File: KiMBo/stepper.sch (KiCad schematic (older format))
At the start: 17 parts

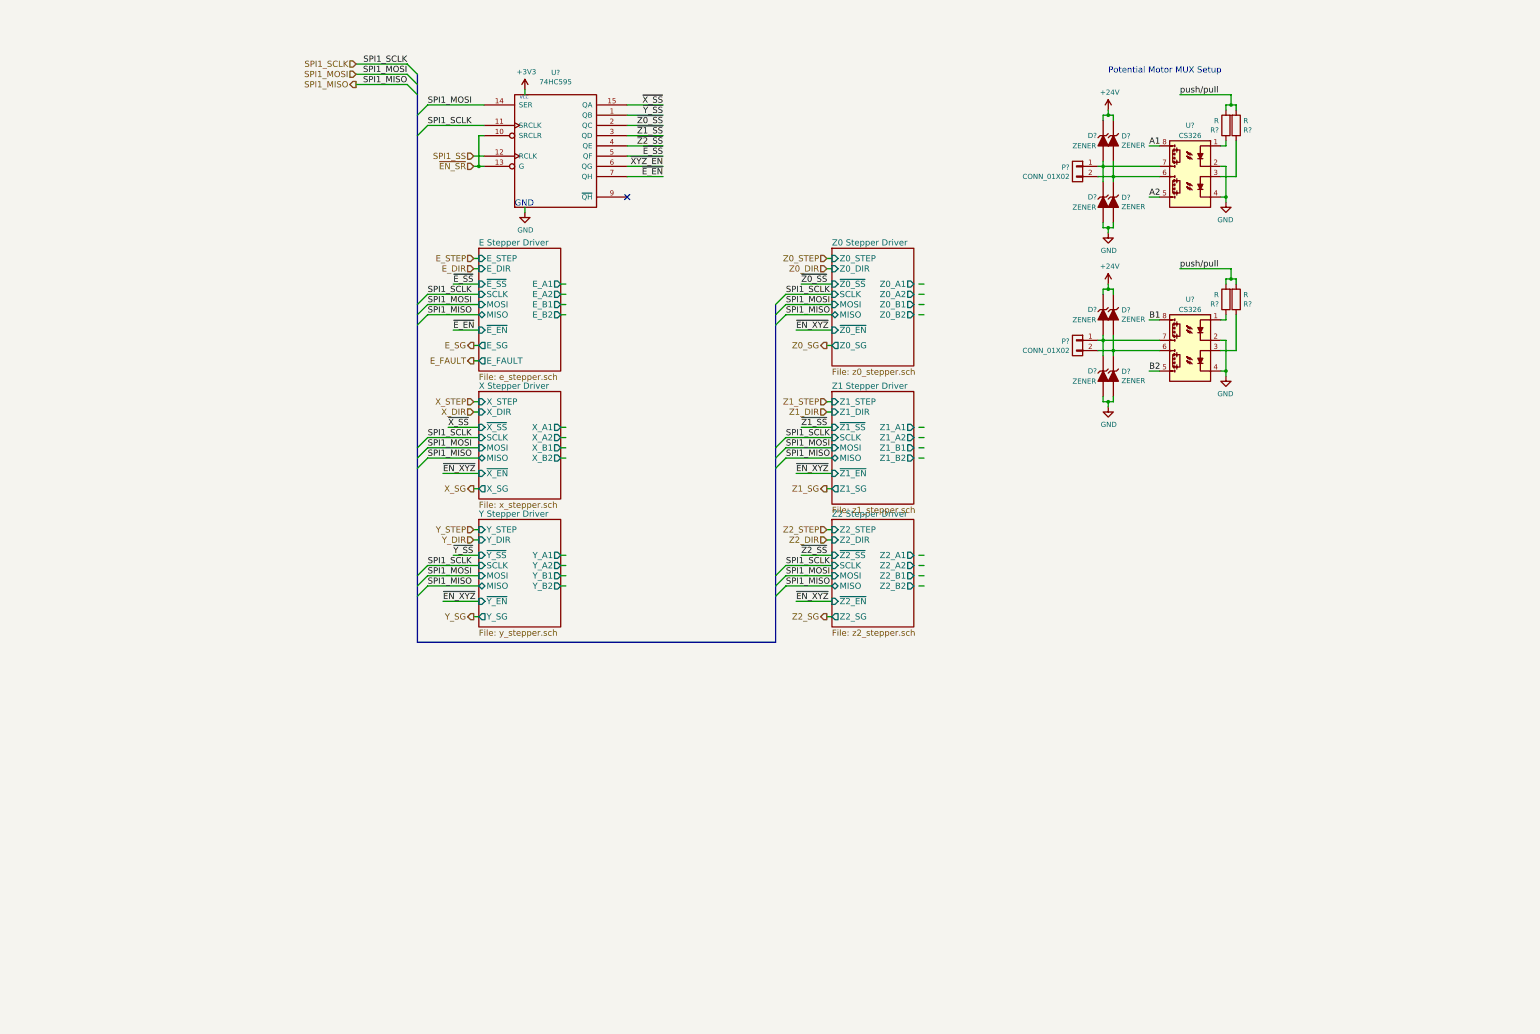
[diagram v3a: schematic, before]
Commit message: Update the fixed Vain voltage and begin placing connectors at the highest level (root) of the hierarchical sheet structure
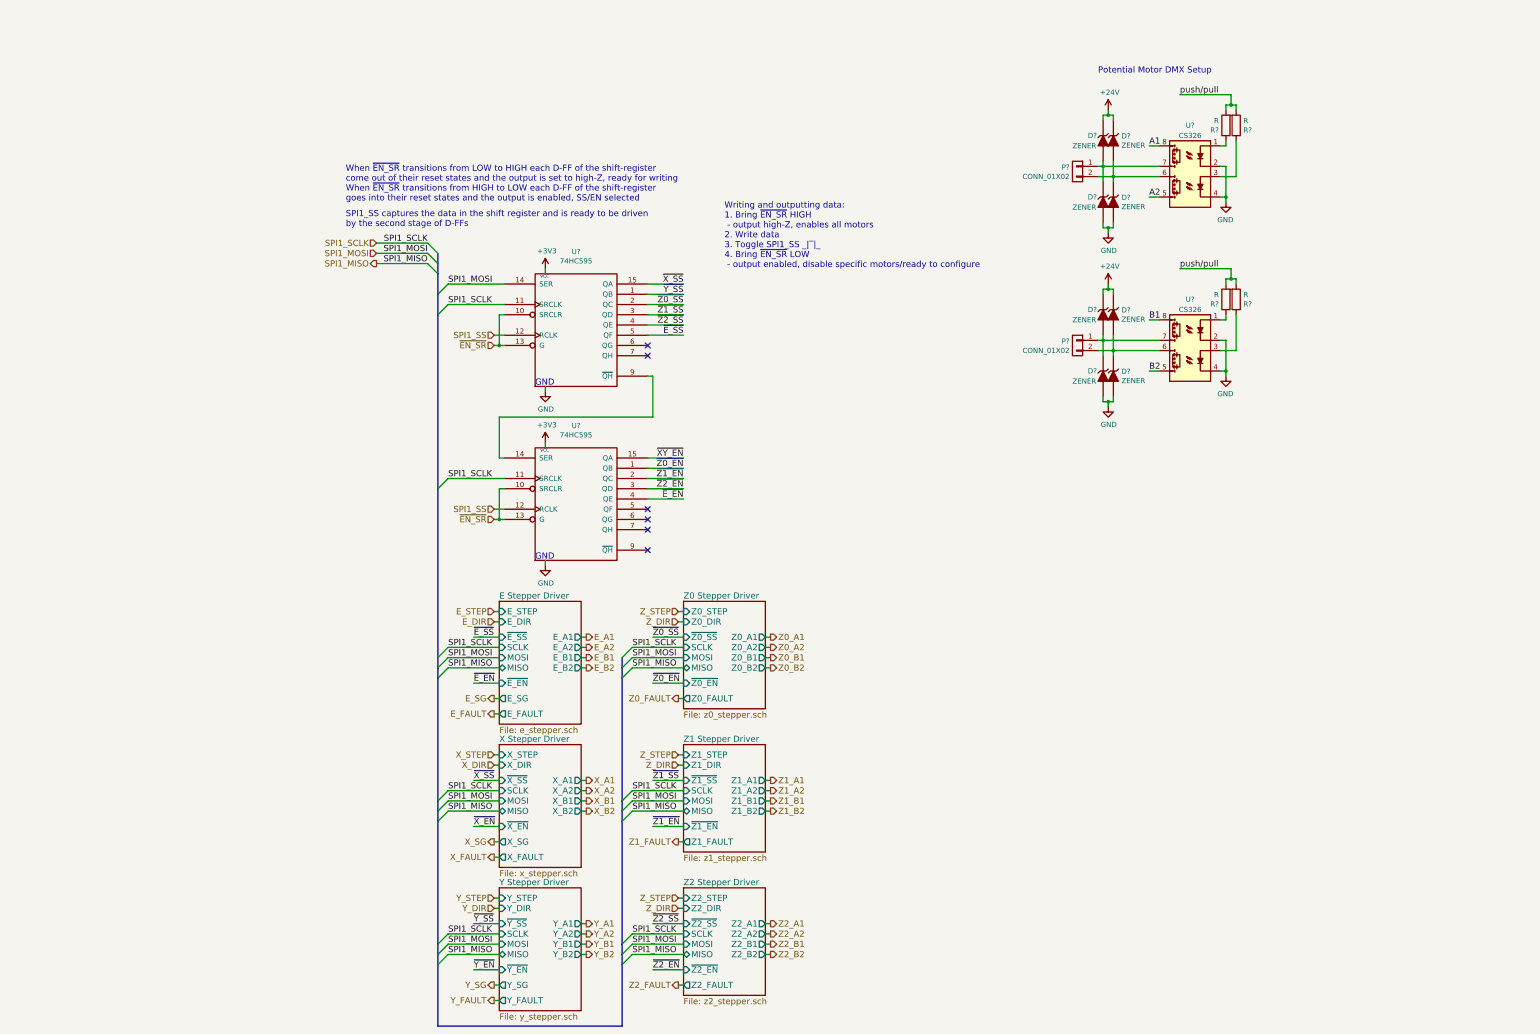
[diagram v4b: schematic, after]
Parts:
- added U?: 74HC595, symbol 74HC595
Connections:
- net labels added: E_A1, E_A2, E_B1, E_B2, X_A1, X_A2, X_B1, X_B2, X_FAULT, Y_A1, Y_A2, Y_B1, Y_B2, Y_FAULT, Z0_A1, Z0_A2, Z0_B1, Z0_B2, Z0_FAULT, Z1_A1, Z1_A2, Z1_B1, Z1_B2, Z1_FAULT, Z2_A1, Z2_A2, Z2_B1, Z2_B2, Z2_FAULT, Z_DIR, Z_STEP, ~XY_EN, ~X_EN, ~Y_EN, ~Z0_EN, ~Z1_EN, ~Z2_EN
- net labels removed: Z0_DIR, Z0_SG, Z0_STEP, Z1_DIR, Z1_SG, Z1_STEP, Z2_DIR, Z2_SG, Z2_STEP, ~EN_XYZ, ~XYZ_EN
- wire segments 161 -> 179
- no-connect marks 1 -> 6
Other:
- note added: "Potential Motor DMX Setup"
- note added: "SPI1_SS captures the data in the shift register and is ready to be driven\nby the second stage of D-FFs"
- note added: "When ~EN_SR~ transitions from LOW to HIGH each D-FF of the shift-register\ncome out of their reset states and the output is set to high-Z, ready for writing\nWhen ~EN_SR~ transitions from HIGH to LOW each D-FF of the shift-register\ngoes into their reset states and the output is enabled, SS/EN selected"
- note added: "Writing and outputting data:\n1. Bring ~EN_SR~ HIGH\n - output high-Z, enables all motors\n2. Write data\n3. Toggle SPI1_SS _|‾|_\n4. Bring ~EN_SR~ LOW\n - output enabled, disable specific motors/ready to configure"
- note removed: "Potential Motor MUX Setup"
- moved on the sheet: U?

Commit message: Bring more interfaces out to the root sheet and begin connecting modules
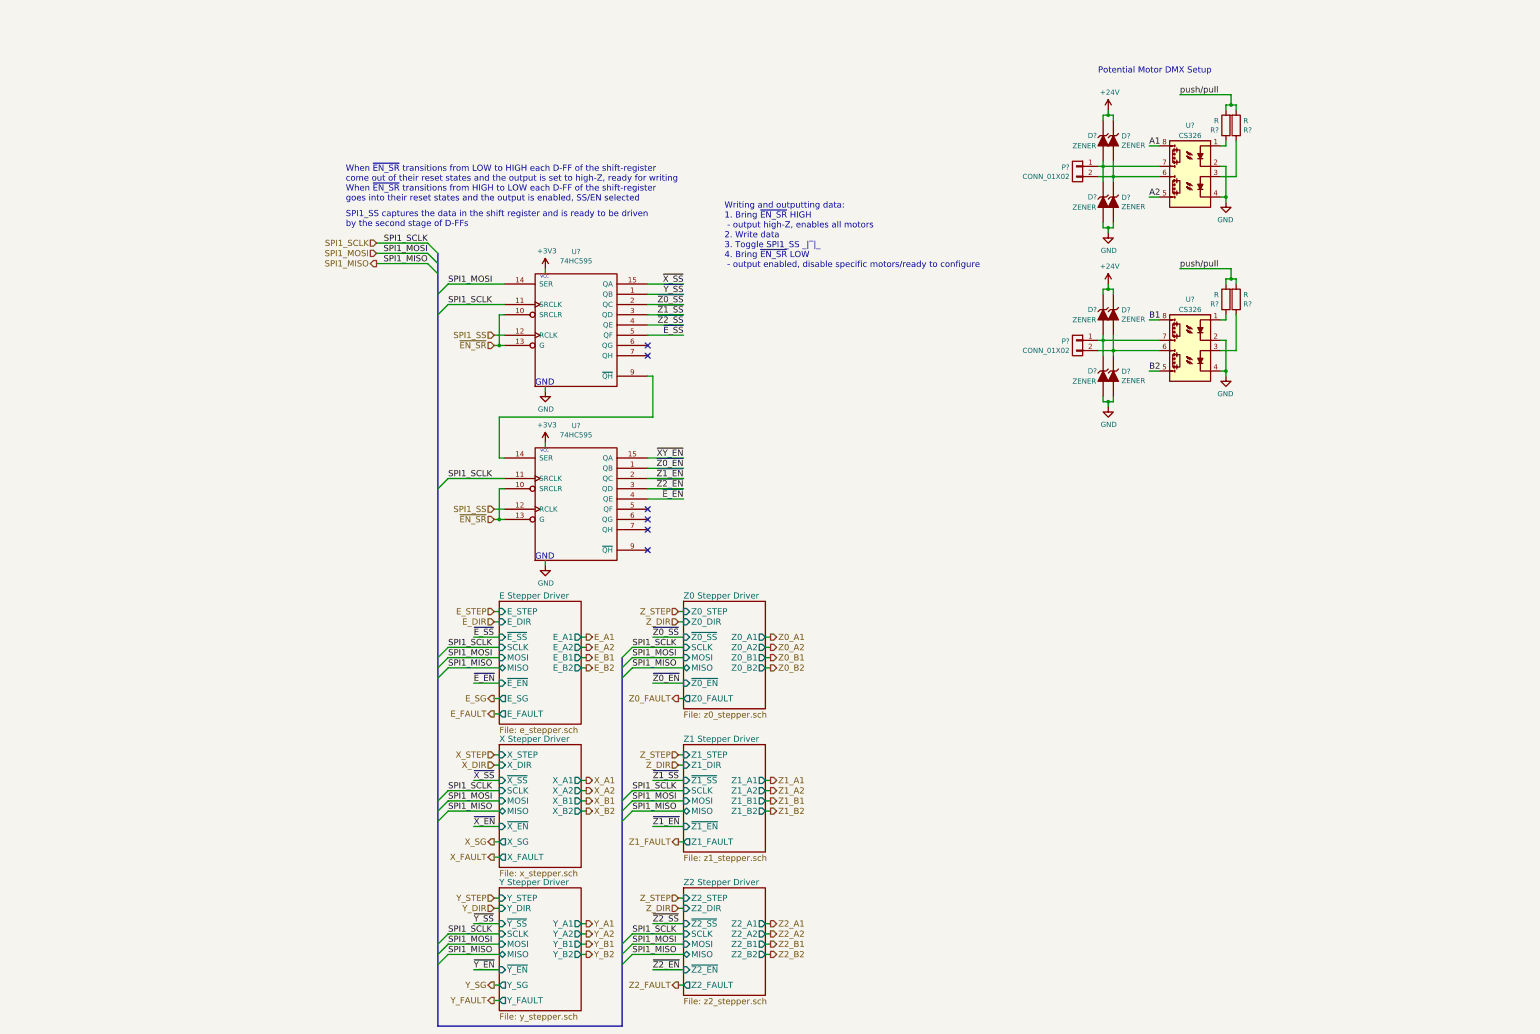
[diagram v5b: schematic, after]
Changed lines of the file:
@@
 $Descr A3 16535 11693
 encoding utf-8
-Sheet 17 23
+Sheet 16 23
 Title ""
 Date ""
@@
 	4900 3450 5450 3450
 Wire Wire Line
-	5350 3850 5400 3850
-Wire Wire Line
-	5400 3850 5450 3850
+	5350 3850 5450 3850
 Wire Wire Line
 	5450 3750 5350 3750
@@
 Connection ~ 11400 3900
 Wire Wire Line
-	11400 3750 11400 3900
-Wire Wire Line
-	11400 3900 11400 3950
+	11400 3750 11400 3950
 Connection ~ 11300 3800
 Wire Wire Line
-	11300 3750 11300 3800
-Wire Wire Line
-	11300 3800 11300 3950
+	11300 3750 11300 3950
 Connection ~ 11350 4400
 Wire Wire Line
 	11350 4450 11350 4400
 Wire Wire Line
-	11300 4400 11350 4400
-Wire Wire Line
-	11350 4400 11400 4400
+	11300 4400 11400 4400
 Wire Wire Line
 	11400 4400 11400 4350
@@
 	11350 3300 11350 3250
 Wire Wire Line
-	11300 3300 11350 3300
-Wire Wire Line
-	11350 3300 11400 3300
+	11300 3300 11400 3300
 Wire Wire Line
 	11400 3300 11400 3350
@@
 	11850 3600 11750 3600
 Wire Wire Line
-	11250 3800 11300 3800
-Wire Wire Line
-	11300 3800 11850 3800
-Wire Wire Line
-	11250 3900 11400 3900
-Wire Wire Line
-	11400 3900 11850 3900
+	11250 3800 11850 3800
+Wire Wire Line
+	11250 3900 11850 3900
 Wire Wire Line
 	12550 3100 12050 3100
@@
 Connection ~ 12550 3200
 Wire Wire Line
-	12500 3200 12550 3200
-Wire Wire Line
-	12550 3200 12600 3200
+	12500 3200 12600 3200
 Wire Wire Line
 	12600 3200 12600 3250
@@
 	12500 3200 12500 3250
 Wire Wire Line
-	12500 3800 12500 4100
-Wire Wire Line
-	12500 4100 12500 4150
+	12500 3800 12500 4150
 Wire Wire Line
 	12450 4100 12500 4100
@@
 Connection ~ 11400 2200
 Wire Wire Line
-	11400 2050 11400 2200
-Wire Wire Line
-	11400 2200 11400 2250
+	11400 2050 11400 2250
 Connection ~ 11300 2100
 Wire Wire Line
-	11300 2050 11300 2100
-Wire Wire Line
-	11300 2100 11300 2250
+	11300 2050 11300 2250
 Connection ~ 11350 2700
 Wire Wire Line
 	11350 2750 11350 2700
 Wire Wire Line
-	11300 2700 11350 2700
-Wire Wire Line
-	11350 2700 11400 2700
+	11300 2700 11400 2700
 Wire Wire Line
 	11400 2700 11400 2650
@@
 	11350 1600 11350 1550
 Wire Wire Line
-	11300 1600 11350 1600
-Wire Wire Line
-	11350 1600 11400 1600
+	11300 1600 11400 1600
 Wire Wire Line
 	11400 1600 11400 1650
@@
 	11850 1900 11750 1900
 Wire Wire Line
-	11250 2100 11300 2100
-Wire Wire Line
-	11300 2100 11850 2100
-Wire Wire Line
-	11250 2200 11400 2200
-Wire Wire Line
-	11400 2200 11850 2200
+	11250 2100 11850 2100
+Wire Wire Line
+	11250 2200 11850 2200
 Wire Wire Line
 	12550 1400 12050 1400
@@
 Connection ~ 12550 1500
 Wire Wire Line
-	12500 1500 12550 1500
-Wire Wire Line
-	12550 1500 12600 1500
+	12500 1500 12600 1500
 Wire Wire Line
 	12600 1500 12600 1550
@@
 	12500 1500 12500 1550
 Wire Wire Line
-	12500 2100 12500 2400
-Wire Wire Line
-	12500 2400 12500 2450
+	12500 2100 12500 2450
 Wire Wire Line
 	12450 2400 12500 2400
@@
 	5400 6450 5350 6450
 Wire Bus Line
-	4800 2950 4800 3050
-Wire Bus Line
-	4800 3050 4800 3150
-Wire Bus Line
-	4800 3150 4800 3350
-Wire Bus Line
-	4800 3350 4800 3550
-Wire Bus Line
-	4800 3550 4800 5250
-Wire Bus Line
-	4800 5250 4800 6900
-Wire Bus Line
-	4800 6900 4800 7000
-Wire Bus Line
-	4800 7000 4800 7100
-Wire Bus Line
-	4800 7100 4800 8300
-Wire Bus Line
-	4800 8300 4800 8400
-Wire Bus Line
-	4800 8400 4800 8500
-Wire Bus Line
-	4800 8500 4800 9700
-Wire Bus Line
-	4800 9700 4800 9800
-Wire Bus Line
-	4800 9800 4800 9900
-Wire Bus Line
-	4800 9900 4800 10500
+	4800 2950 4800 10500
 Wire Wire Line
 	4900 7000 5400 7000
@@
 	4900 6800 5400 6800
 Wire Bus Line
-	6600 6900 6600 7000
-Wire Bus Line
-	6600 7000 6600 7100
-Wire Bus Line
-	6600 7100 6600 8300
-Wire Bus Line
-	6600 8300 6600 8400
-Wire Bus Line
-	6600 8400 6600 8500
-Wire Bus Line
-	6600 8500 6600 9700
-Wire Bus Line
-	6600 9700 6600 9800
-Wire Bus Line
-	6600 9800 6600 9900
-Wire Bus Line
-	6600 9900 6600 10500
+	6600 6900 6600 10500
 Wire Bus Line
 	6600 10500 4800 10500
@@
 	4900 5150 5450 5150
 Wire Wire Line
-	5350 5550 5400 5550
-Wire Wire Line
-	5400 5550 5450 5550
+	5350 5550 5450 5550
 Wire Wire Line
 	5450 5450 5350 5450
